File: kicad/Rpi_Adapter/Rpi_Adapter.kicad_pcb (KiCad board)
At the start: 2 copper layers, 39.3 x 76 mm, 46 parts, among them P1 CONN_02X20, P2 CONN_02X03

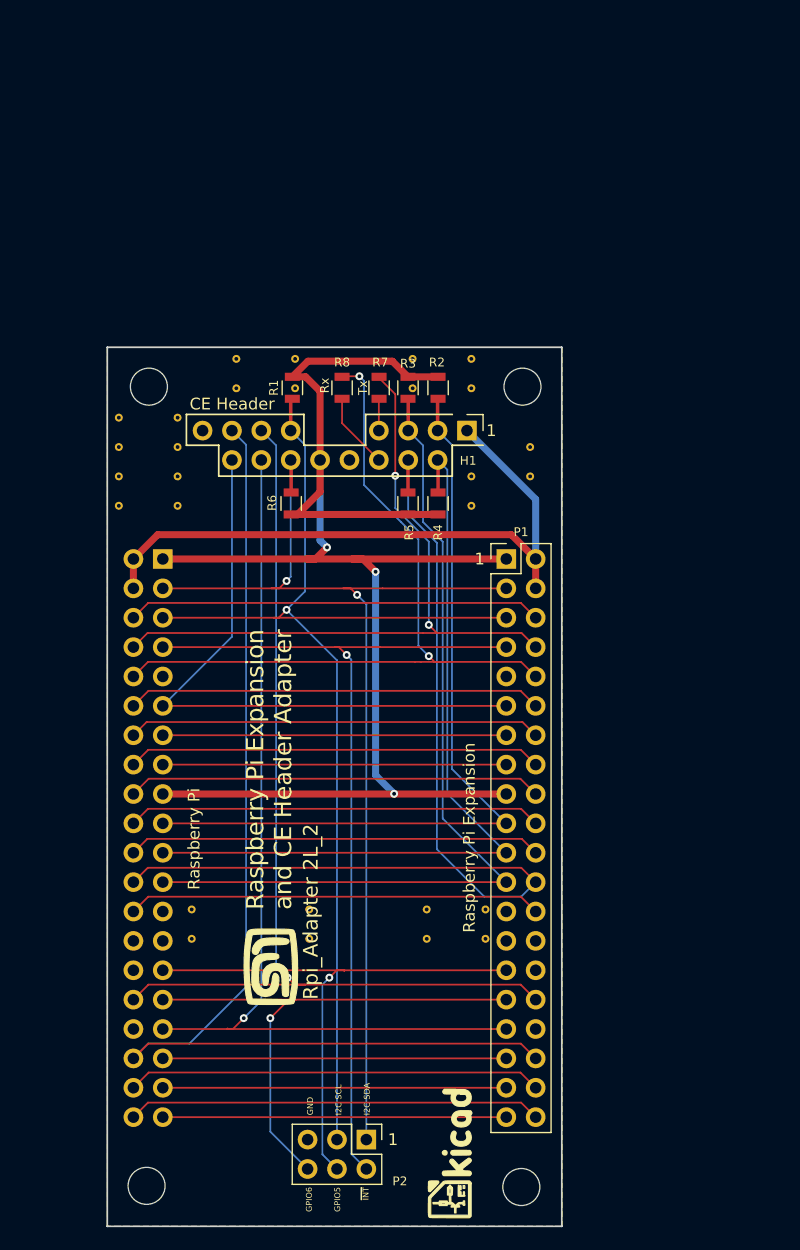
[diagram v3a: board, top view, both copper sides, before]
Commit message: Re-worked the RPi Adapter to be more compact.
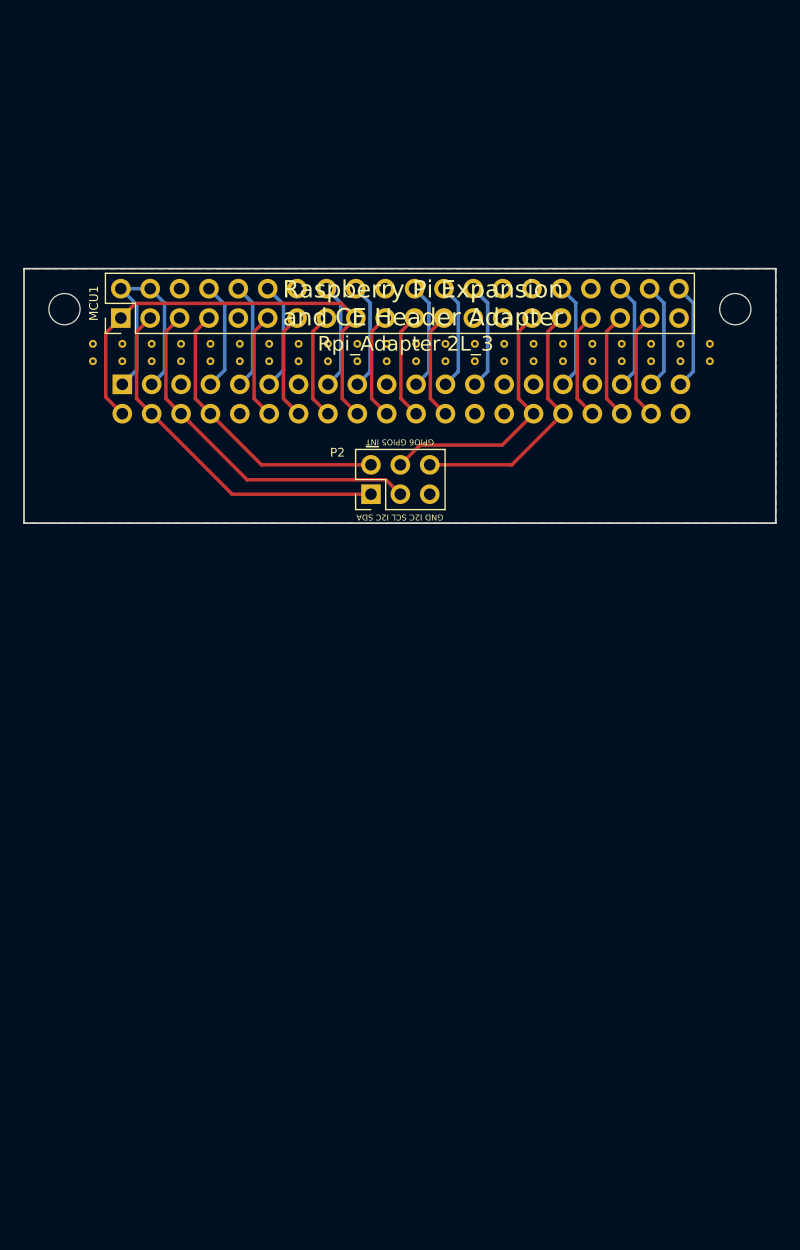
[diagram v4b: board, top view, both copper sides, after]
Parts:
- removed the 1 at (170.5, 97.4)
- removed ? (x20): Stitch, Rpi_Adapter_Footprints:Stitch
- removed ? (x4): MountingHole_3.2mm_M3, Mounting_Holes:MountingHole_3.2mm_M3
- removed ?: LOGO, Rpi_Adapter_Footprints:KiCad-Logo
- removed G***: LOGO, Rpi_Adapter_Footprints:MyBasic_rounded_50_1
- removed H1: CE_Header, CE_Header:CE_Header
- removed R1, R2, R3, R4, R5, R6: 4k7, Resistors_SMD:R_0805
- removed R7, R8: 0, Resistors_SMD:R_0805
- added 1: Stitch, Rpi_Adapter_Footprints:Stitch, F.Cu at (162.0, 48.5)
- added 1: Stitch, Rpi_Adapter_Footprints:Stitch, F.Cu at (164.5, 48.5)
- added 10: Stitch, Rpi_Adapter_Footprints:Stitch, F.Cu at (187.4, 48.5)
- added 13: Stitch, Rpi_Adapter_Footprints:Stitch, F.Cu at (195.0, 48.5)
- added 14: Stitch, Rpi_Adapter_Footprints:Stitch, F.Cu at (197.5, 48.5)
- added 15: Stitch, Rpi_Adapter_Footprints:Stitch, F.Cu at (200.1, 48.5)
- added 16: Stitch, Rpi_Adapter_Footprints:Stitch, F.Cu at (202.6, 48.5)
- added 17: Stitch, Rpi_Adapter_Footprints:Stitch, F.Cu at (205.1, 48.5)
- added 18: Stitch, Rpi_Adapter_Footprints:Stitch, F.Cu at (207.7, 48.5)
- added 19: Stitch, Rpi_Adapter_Footprints:Stitch, F.Cu at (210.2, 48.5)
- added 2: Stitch, Rpi_Adapter_Footprints:Stitch, F.Cu at (167.0, 48.5)
- added 20: Stitch, Rpi_Adapter_Footprints:Stitch, F.Cu at (215.3, 48.5)
- added 20: Stitch, Rpi_Adapter_Footprints:Stitch, F.Cu at (212.8, 48.5)
- added 21: Stitch, Rpi_Adapter_Footprints:Stitch, F.Cu at (162.0, 50.0)
- added 21: Stitch, Rpi_Adapter_Footprints:Stitch, F.Cu at (164.5, 50.0)
- added 22: Stitch, Rpi_Adapter_Footprints:Stitch, F.Cu at (167.0, 50.0)
- added 23: Stitch, Rpi_Adapter_Footprints:Stitch, F.Cu at (169.6, 50.0)
- added 24: Stitch, Rpi_Adapter_Footprints:Stitch, F.Cu at (172.1, 50.0)
- added 25: Stitch, Rpi_Adapter_Footprints:Stitch, F.Cu at (174.7, 50.0)
- added 26: Stitch, Rpi_Adapter_Footprints:Stitch, F.Cu at (177.2, 50.0)
- added 27: Stitch, Rpi_Adapter_Footprints:Stitch, F.Cu at (179.7, 50.0)
- added 28: Stitch, Rpi_Adapter_Footprints:Stitch, F.Cu at (182.3, 50.0)
- added 29: Stitch, Rpi_Adapter_Footprints:Stitch, F.Cu at (184.8, 50.0)
- added 30: Stitch, Rpi_Adapter_Footprints:Stitch, F.Cu at (187.4, 50.0)
- added 31: Stitch, Rpi_Adapter_Footprints:Stitch, F.Cu at (189.9, 50.0)
- added 32: Stitch, Rpi_Adapter_Footprints:Stitch, F.Cu at (192.4, 50.0)
- added 33: Stitch, Rpi_Adapter_Footprints:Stitch, F.Cu at (195.0, 50.0)
- added 34: Stitch, Rpi_Adapter_Footprints:Stitch, F.Cu at (197.5, 50.0)
- added 35: Stitch, Rpi_Adapter_Footprints:Stitch, F.Cu at (200.1, 50.0)
- added 36: Stitch, Rpi_Adapter_Footprints:Stitch, F.Cu at (202.6, 50.0)
- added 37: Stitch, Rpi_Adapter_Footprints:Stitch, F.Cu at (205.1, 50.0)
- added 38: Stitch, Rpi_Adapter_Footprints:Stitch, F.Cu at (207.7, 50.0)
- added 39: Stitch, Rpi_Adapter_Footprints:Stitch, F.Cu at (210.2, 50.0)
- added 4: Stitch, Rpi_Adapter_Footprints:Stitch, F.Cu at (172.1, 48.5)
- added 40: Stitch, Rpi_Adapter_Footprints:Stitch, F.Cu at (215.3, 50.0)
- added 40: Stitch, Rpi_Adapter_Footprints:Stitch, F.Cu at (212.8, 50.0)
- added 8: Stitch, Rpi_Adapter_Footprints:Stitch, F.Cu at (182.3, 48.5)
- added MNT**: MountingHole_2.7mm_M2.5, Mounting_Holes:MountingHole_2.7mm_M2.5, F.Cu at (217.5, 45.5)
- added MNT**: MountingHole_2.7mm_M2.5, Mounting_Holes:MountingHole_2.7mm_M2.5, F.Cu at (159.5, 45.5)
- MCU1: moved to F.Cu
- P1: moved to B.Cu
- moved P2 55.8 mm to (186.0, 61.5), turned to 90 degrees
- moved 6 52.4 mm to (177.2, 48.5)
- moved 7 52.3 mm to (179.7, 48.5)
- moved 9 51.6 mm to (184.8, 48.5)
- moved 12 51.6 mm to (192.4, 48.5)
- moved 5 51.5 mm to (174.7, 48.5)
- moved 11 51.4 mm to (189.9, 48.5)
- moved 3 50.1 mm to (169.6, 48.5)
- moved P1 36.5 mm to (164.5, 52.0), turned to 270 degrees
- moved MCU1 21.1 mm to (164.4, 46.3), turned to 90 degrees
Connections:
- MCU1 pad 27: Net-(MCU1-Pad27) -> (no net)
- MCU1 pad 28: Net-(MCU1-Pad28) -> (no net)
- P1 pad 1: /3V3 -> /5V
- P1 pad 10: /UART0_Rx -> GND
- P1 pad 11: /GPIO_17 -> /GPIO_18
- P1 pad 12: /GPIO_18 -> /GPIO_17
- P1 pad 13: /GPIO_27 -> GND
- P1 pad 14: GND -> /GPIO_27
- P1 pad 15: /GPIO_22 -> /GPIO_23
- P1 pad 16: /GPIO_23 -> /GPIO_22
- P1 pad 17: /3V3 -> /GPIO_24
- P1 pad 18: /GPIO_24 -> /3V3
- P1 pad 19: /SPI0_MOSI -> GND
- P1 pad 2: /5V -> /3V3
- P1 pad 20: GND -> /SPI0_MOSI
- P1 pad 21: /SPI0_MISO -> /GPIO_25
- P1 pad 22: /GPIO_25 -> /SPI0_MISO
- P1 pad 23: /SPI0_SCLK -> /SPI0_CS0
- P1 pad 24: /SPI0_CS0 -> /SPI0_SCLK
- P1 pad 25: GND -> /SPI0_CS1
- P1 pad 26: /SPI0_CS1 -> GND
- P1 pad 27: Net-(P1-Pad27) -> (no net)
- P1 pad 28: Net-(P1-Pad28) -> (no net)
- P1 pad 29: /GPIO_5 -> GND
- P1 pad 3: /I2C1_SDA -> /5V
- P1 pad 30: GND -> /GPIO_5
- P1 pad 31: /GPIO_6 -> /GPIO_12
- P1 pad 32: /GPIO_12 -> /GPIO_6
- P1 pad 33: /GPIO_13 -> GND
- P1 pad 34: GND -> /GPIO_13
- P1 pad 35: /GPIO_19 -> /GPIO_16
- P1 pad 36: /GPIO_16 -> /GPIO_19
- P1 pad 37: /GPIO_26 -> /GPIO_20
- P1 pad 38: /GPIO_20 -> /GPIO_26
- P1 pad 39: GND -> /GPIO_21
- P1 pad 4: /5V -> /I2C1_SDA
- P1 pad 40: /GPIO_21 -> GND
- P1 pad 5: /I2C1_SCL -> GND
- P1 pad 6: GND -> /I2C1_SCL
- P1 pad 7: /GPIO_4 -> /UART0_Tx
- P1 pad 8: /UART0_Tx -> /GPIO_4
- P1 pad 9: GND -> /UART0_Rx
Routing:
- net GND: track 137.1 -> 0.00 mm
- net /3V3: track 133.0 -> 40.1 mm, vias 3 -> 0
- net /GPIO_16: track 96.7 -> 9.24 mm
- net /GPIO_12: track 85.8 -> 9.24 mm, vias 1 -> 0
- net /SPI0_CS0: track 84.1 -> 9.24 mm
- net /GPIO_13: track 80.4 -> 9.30 mm, vias 1 -> 0
- net /I2C1_SCL: track 98.2 -> 31.1 mm, vias 1 -> 0
- net /SPI0_SCLK: track 75.0 -> 9.30 mm
- net /I2C1_SDA: track 93.5 -> 31.1 mm, vias 2 -> 0
- net /SPI0_MISO: track 68.9 -> 9.30 mm
- net /SPI0_MOSI: track 68.9 -> 9.30 mm
- net /UART0_Rx: track 65.6 -> 9.24 mm, vias 2 -> 0
- net /GPIO_4: track 76.2 -> 25.0 mm, vias 1 -> 0
- net /UART0_Tx: track 60.1 -> 9.35 mm, vias 2 -> 0
- net /GPIO_17: track 53.4 -> 9.30 mm
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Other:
- board size 39.3 x 76 mm -> 65 x 22 mm
- board text added: "Rpi_Adapter 2L_3"
- board text removed: "1"
- board text removed: "CE Header"
- board text removed: "Raspberry Pi"
- board text removed: "Raspberry Pi Expansion"
- board text removed: "Rpi_Adapter 2L_2"
- board text removed: "Rx"
- board text removed: "Tx"

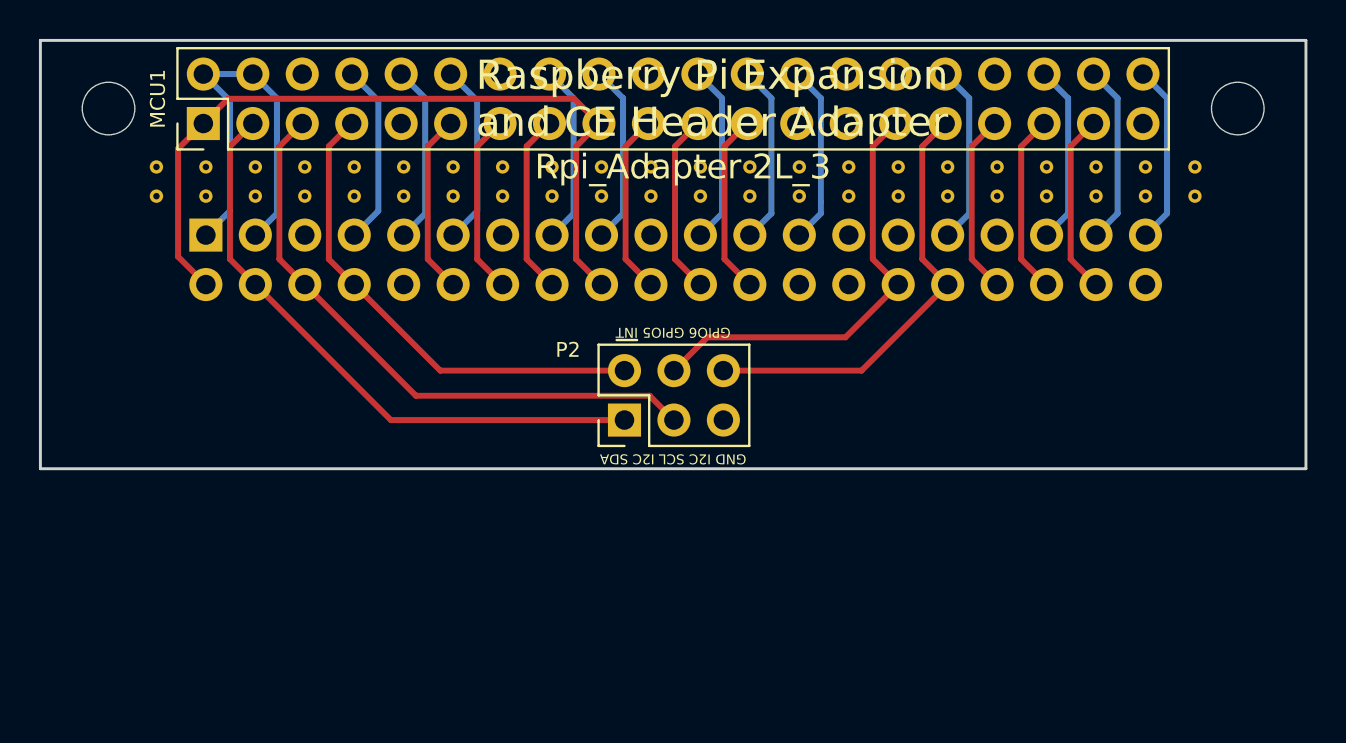
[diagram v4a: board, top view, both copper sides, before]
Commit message: Reworked the RPi Adapter 2L_4 for RJ45
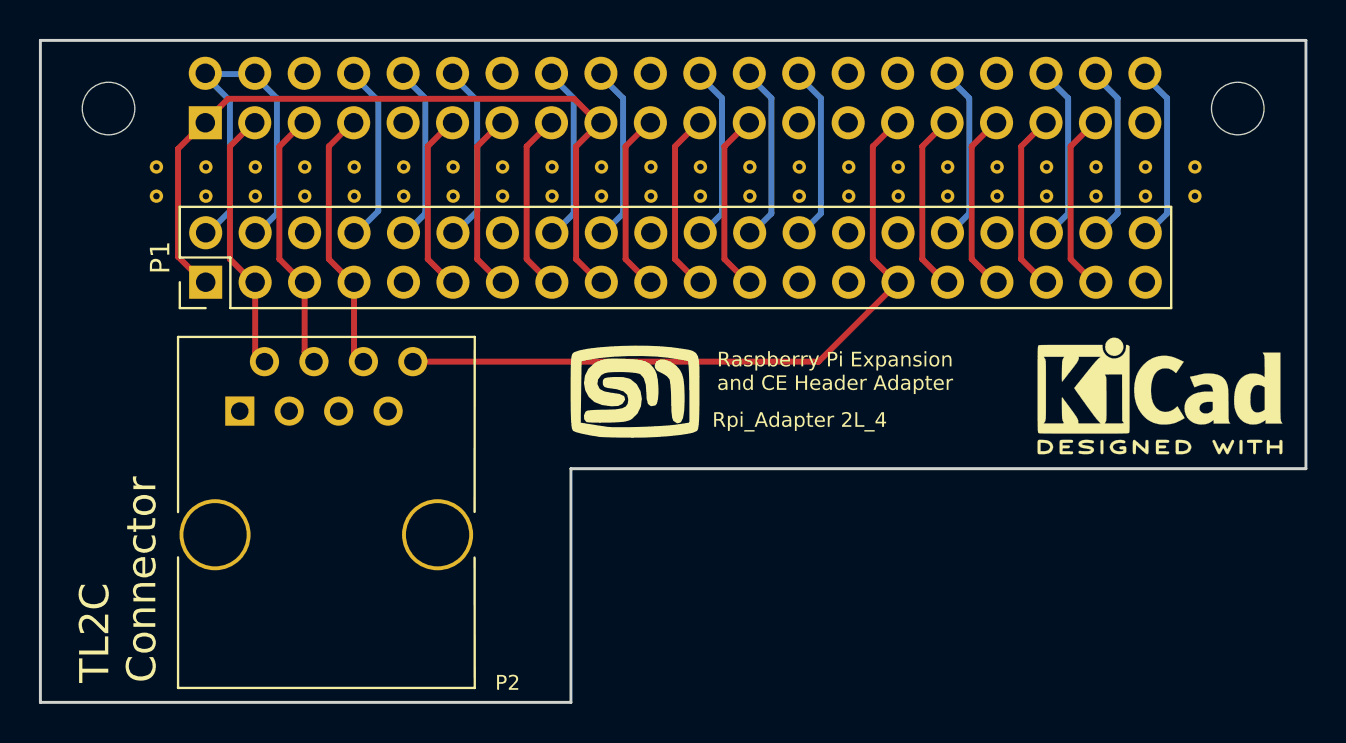
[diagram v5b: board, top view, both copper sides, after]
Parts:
- added G***: LOGO, Rpi_Adapter_Footprints:MyBasic_rounded_50_1, F.Cu at (186.5, 60.0)
- added REF***: KiCad-Logo2_6mm_SilkScreen, Symbols:KiCad-Logo2_6mm_SilkScreen, F.Cu at (213.5, 60.2)
- MCU1: footprint Rpi_Adapter_Footprints:Pin_Header_Straight_2x20_Pitch2.54mm -> Socket_Strips:Socket_Strip_Straight_2x20_Pitch2.54mm; moved to B.Cu
- P1: moved to F.Cu
- P2: value CONN_02X03 -> CONN_01X08; footprint Pin_Headers:Pin_Header_Straight_2x03_Pitch2.54mm -> tl2c-footprint:RJ45_8P8C
- moved P2 11.3 mm to (175.1, 58.5), turned to 0 degrees
- moved P1 2.42 mm to (164.5, 54.4), turned to 90 degrees
- moved MCU1 0.11 mm to (164.5, 46.2), turned to 270 degrees
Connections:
- P1 pad 1: /5V -> /3V3
- P1 pad 10: GND -> /UART0_Rx
- P1 pad 11: /GPIO_18 -> /GPIO_17
- P1 pad 12: /GPIO_17 -> /GPIO_18
- P1 pad 13: GND -> /GPIO_27
- P1 pad 14: /GPIO_27 -> GND
- P1 pad 15: /GPIO_23 -> /GPIO_22
- P1 pad 16: /GPIO_22 -> /GPIO_23
- P1 pad 17: /GPIO_24 -> /3V3
- P1 pad 18: /3V3 -> /GPIO_24
- P1 pad 19: GND -> /SPI0_MOSI
- P1 pad 2: /3V3 -> /5V
- P1 pad 20: /SPI0_MOSI -> GND
- P1 pad 21: /GPIO_25 -> /SPI0_MISO
- P1 pad 22: /SPI0_MISO -> /GPIO_25
- P1 pad 23: /SPI0_CS0 -> /SPI0_SCLK
- P1 pad 24: /SPI0_SCLK -> /SPI0_CS0
- P1 pad 25: /SPI0_CS1 -> GND
- P1 pad 26: GND -> /SPI0_CS1
- P1 pad 29: GND -> /GPIO_5
- P1 pad 3: /5V -> /I2C1_SDA
- P1 pad 30: /GPIO_5 -> GND
- P1 pad 31: /GPIO_12 -> /GPIO_6
- P1 pad 32: /GPIO_6 -> /GPIO_12
- P1 pad 33: GND -> /GPIO_13
- P1 pad 34: /GPIO_13 -> GND
- P1 pad 35: /GPIO_16 -> /GPIO_19
- P1 pad 36: /GPIO_19 -> /GPIO_16
- P1 pad 37: /GPIO_20 -> /GPIO_26
- P1 pad 38: /GPIO_26 -> /GPIO_20
- P1 pad 39: /GPIO_21 -> GND
- P1 pad 4: /I2C1_SDA -> /5V
- P1 pad 40: GND -> /GPIO_21
- P1 pad 5: GND -> /I2C1_SCL
- P1 pad 6: /I2C1_SCL -> GND
- P1 pad 7: /UART0_Tx -> /GPIO_4
- P1 pad 8: /GPIO_4 -> /UART0_Tx
- P1 pad 9: /UART0_Rx -> GND
- P2 pad 1: /I2C1_SDA -> GND
- P2 pad 2: /GPIO_4 -> /I2C1_SDA
- P2 pad 3: /I2C1_SCL -> GND
- P2 pad 4: /GPIO_5 -> /I2C1_SCL
- P2 pad 6: /GPIO_6 -> /GPIO_4
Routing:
- net /I2C1_SDA: track 31.1 -> 13.6 mm
- net /I2C1_SCL: track 31.1 -> 13.6 mm
- net /GPIO_6: track 22.6 -> 9.30 mm
- net /GPIO_5: track 22.6 -> 35.9 mm
- net /GPIO_4: track 25.0 -> 13.6 mm
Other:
- board size 65 x 22 mm -> 65 x 34 mm
- board text added: "Rpi_Adapter 2L_4"
- board text added: "TL2C Connector"
- board text removed: "GND I2C SCL I2C SDA"
- board text removed: "GPIO6 GPIO5 ~INT"
- board text removed: "Rpi_Adapter 2L_3"

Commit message: Enhancements to the RPi Adapter and DIN boards
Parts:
- P2: moved to B.Cu
- moved P2 19.8 mm to (174.6, 38.8)
- renumbered 20 to ?, 35 to ?, 34 to ?, 33 to ?, 32 to ?, 31 to ?, 30 to ?, 29 to ?, 28 to ?, 27 to ?, 26 to ?, 40 to ?, 25 to ?, 24 to ?, 23 to ?, 22 to ?, 21 to ?, 19 to ?, 18 to ?, 17 to ?, 16 to ?, 1 to ?, 15 to ?, 14 to ?, 13 to ?, 12 to ?, 11 to ?, 10 to ?, 9 to ?, 8 to ?, 7 to ?, 6 to ?, 5 to ?, 4 to ?, 3 to ?, 2 to ?, 39 to ?, 38 to ?, 37 to ?, 36 to ?
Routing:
- net /I2C1_SDA: track 13.6 -> 18.5 mm
- net /GPIO_4: track 13.6 -> 17.9 mm
- net /I2C1_SCL: track 13.6 -> 17.9 mm
- net /GPIO_5: track 35.9 -> 38.9 mm
- net /3V3: track 40.1 -> 42.1 mm
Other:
- board size 65 x 34 mm -> 64.9 x 43.2 mm
- board text added: "Rpi_Adapter 2L_5"
- board text removed: "Rpi_Adapter 2L_4"

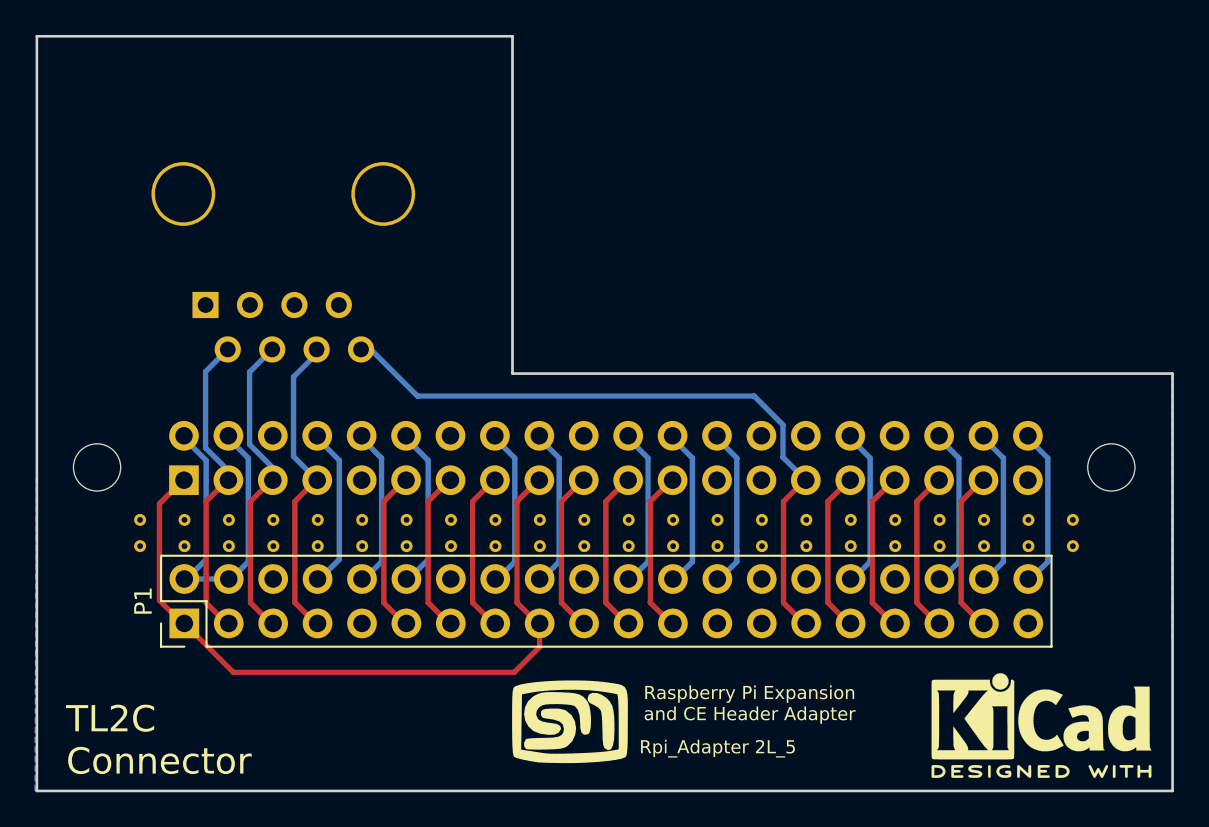
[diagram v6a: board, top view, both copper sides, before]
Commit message: Reduced the size of the Rpi_Adapter to make a better fit into the enclosure
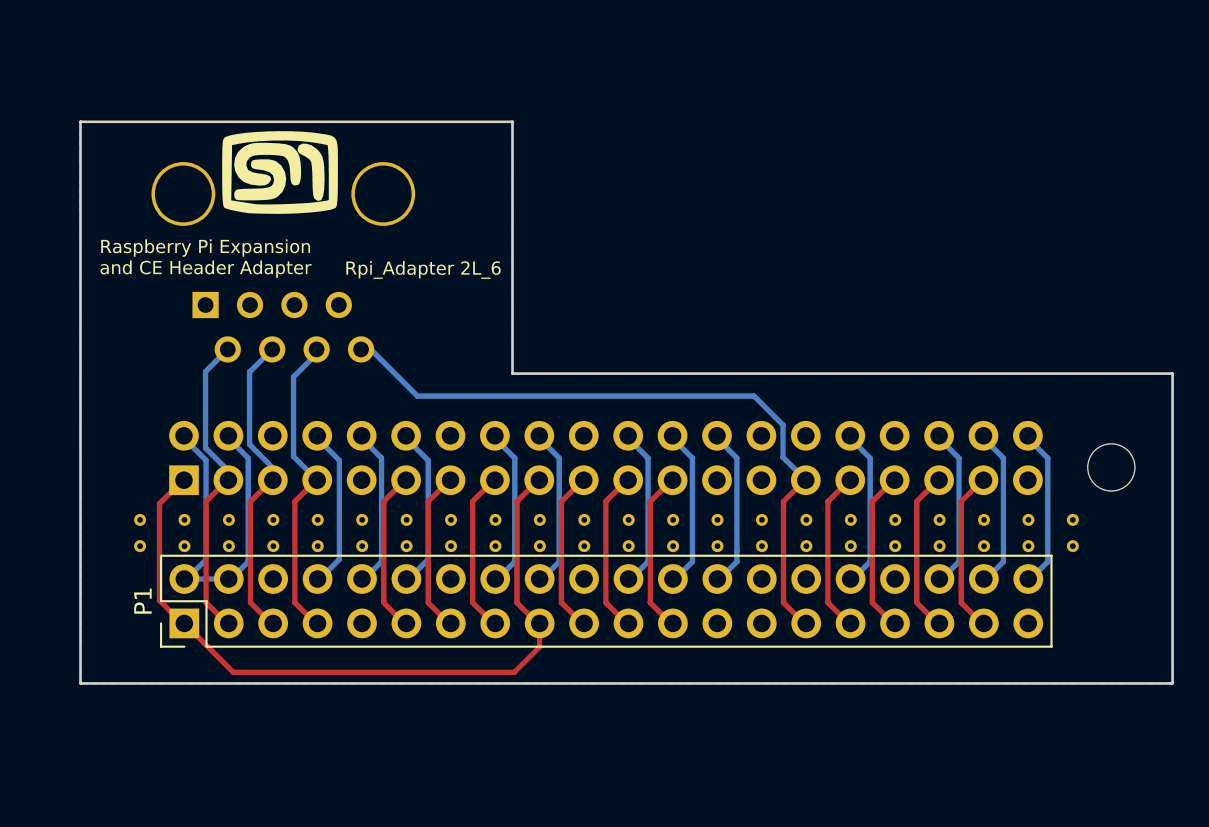
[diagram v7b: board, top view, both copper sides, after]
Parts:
- removed the MNT** at (159.5, 45.5)
- removed REF***: KiCad-Logo2_6mm_SilkScreen, Symbols:KiCad-Logo2_6mm_SilkScreen
- moved G*** 35.5 mm to (169.9, 28.6)
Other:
- board size 64.9 x 43.2 mm -> 62.4 x 32.1 mm
- board text added: "Rpi_Adapter 2L_6"
- board text removed: "Rpi_Adapter 2L_5"
